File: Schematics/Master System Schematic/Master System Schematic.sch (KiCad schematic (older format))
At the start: 42 parts, among them J1 +12V, J12 BMS 12V, J13 Charger BMS 12V, J2 Charger +12V, J3 GND, J4 Charger GND, J5 TS+, J6 TS-, K1 Cooling Pump Relay, M1 Cooling Pump, SW1 SideMounted (BRB), SW10 SMD, SW11 BRAKE_SWITCH, SW12 SW_SPST_Pressure, SW13 SW_SPST_Pressure, SW2 SideMounted (BRB), SW3 GLVMS, SW4 Brake Over-Travel Switch, SW5 Latching Circuit Reset, SW6 Cockpit Shutdown (BRB), SW7 TSMS, SW8 SMD, SW9 HVD, U1 FuseBox_PSZACCEPS052H, U2 Bender_Isometer_IR155-3204, U3 RinehartPM100DX_MotorControll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, U4 Emrax228HV_Motor

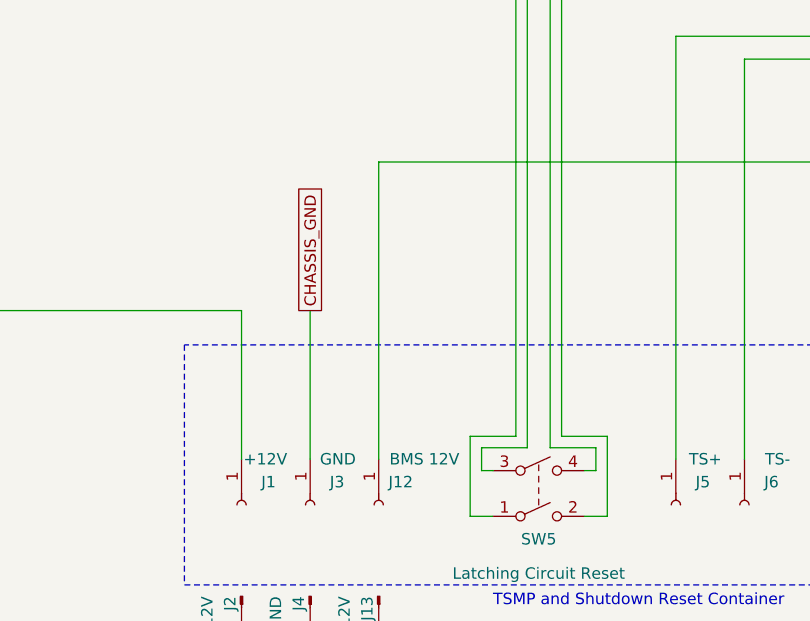
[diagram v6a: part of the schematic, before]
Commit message: Added fuse
Probably a good idea
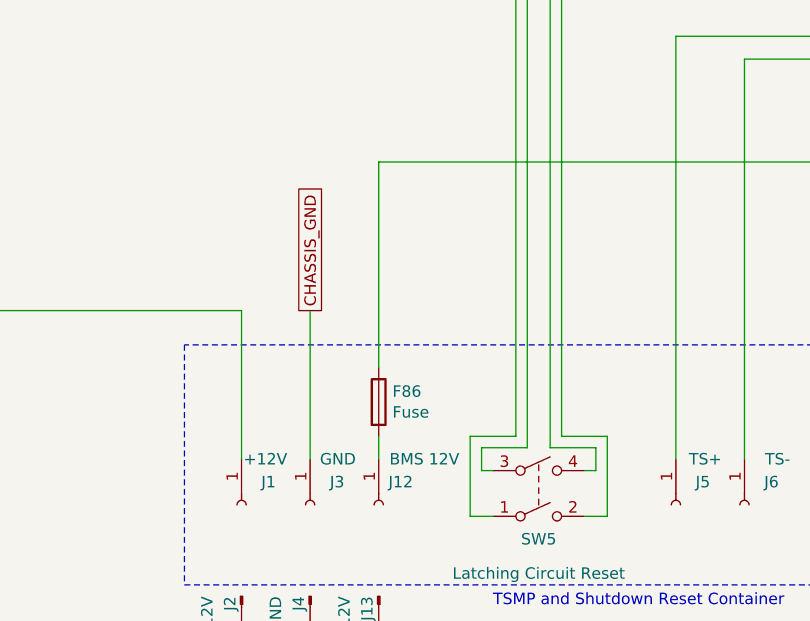
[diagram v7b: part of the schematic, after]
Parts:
- added F86: Fuse, symbol Device:Fuse
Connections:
- net BMS Container/ChargerPWR: now also F86.1; no longer J12.1 (Pin_1)
- new net: U1.6, U3.23 (CANB_H), U3.8 (Reverse_Enable_Switch)
- new net: F86.2, J12.1 (Pin_1)
- new net: U3.~ (TS-), U4.~ (AC3) (x2)
- now unconnected: U3.23 (CANB_H), U3.8 (Reverse_Enable_Switch)
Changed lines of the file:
@@
 Wire Wire Line
 	9500 7850 4250 7850
-Wire Wire Line
-	4250 7850 4250 9150
 $Comp
 L Connector:Conn_01x01_Female J12
@@
 Wire Wire Line
 	4250 9950 4250 10300
+Connection ~ 4250 10300
+Wire Wire Line
+	4250 10300 8550 10300
+$Comp
+L Device:Fuse F86
+U 1 1 5F9E6519
+P 4250 8900
+F 0 "F86" H 4310 8946 50  0000 L CNN
+F 1 "Fuse" H 4310 8855 50  0000 L CNN
+F 2 "" V 4180 8900 50  0001 C CNN
+F 3 "~" H 4250 8900 50  0001 C CNN
+	1    4250 8900
+	1    0    0    -1
+$EndComp
+Wire Wire Line
+	4250 9150 4250 9050
+Wire Wire Line
+	4250 8750 4250 7850
 Wire Bus Line
 	11300 3250 11300 3600
@@
 Wire Bus Line
 	12050 800  12050 6750
-Connection ~ 4250 10300
-Wire Wire Line
-	4250 10300 8550 10300
 $EndSCHEMATC
